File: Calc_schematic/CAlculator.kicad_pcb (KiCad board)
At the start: 2 copper layers, 1 part, among them U2 LCD-016N002L

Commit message: last mod
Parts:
- added J1: Conn_01x02_Female, Connector_JST:JST_PH_B2B-PH-K_1x02_P2.00mm_Vertical, F.Cu at (63.2, 25.2)
- added SW0: SW_Push, Button_Switch_THT:SW_PUSH_6mm_H5mm, F.Cu at (40.8, 109.5)
- added SW1: SW_Push, Button_Switch_THT:SW_PUSH_6mm_H5mm, F.Cu at (40.5, 123.2)
- added SW10: SW_Push, Button_Switch_THT:SW_PUSH_6mm_H5mm, F.Cu at (86.0, 109.5)
- added SW11: SW_Push, Button_Switch_THT:SW_PUSH_6mm_H5mm, F.Cu at (86.2, 123.2)
- added SW12: SW_Push, Button_Switch_THT:SW_PUSH_6mm_H5mm, F.Cu at (86.2, 137.5)
- added SW13: SW_Push, Button_Switch_THT:SW_PUSH_6mm_H5mm, F.Cu at (86.2, 152.2)
- added SW14: SW_Push, Button_Switch_THT:SW_PUSH_6mm_H5mm, F.Cu at (86.5, 166.0)
- added SW15: SW_Push, Button_Switch_THT:SW_PUSH_6mm_H5mm, F.Cu at (106.2, 109.5)
- added SW16: SW_Push, Button_Switch_THT:SW_PUSH_6mm_H5mm, F.Cu at (106.2, 123.2)
- added SW17: SW_Push, Button_Switch_THT:SW_PUSH_6mm_H5mm, F.Cu at (106.2, 137.5)
- added SW18: SW_Push, Button_Switch_THT:SW_PUSH_6mm_H5mm, F.Cu at (106.0, 152.2)
- added SW19: SW_Push, Button_Switch_THT:SW_PUSH_6mm_H5mm, F.Cu at (105.8, 166.0)
- added SW2: SW_Push, Button_Switch_THT:SW_PUSH_6mm_H5mm, F.Cu at (40.5, 137.8)
- added SW20: SW_Push, Button_Switch_THT:SW_PUSH_6mm_H5mm, F.Cu at (129.5, 109.8)
- added SW21: SW_Push, Button_Switch_THT:SW_PUSH_6mm_H5mm, F.Cu at (129.2, 123.2)
- added SW22: SW_Push, Button_Switch_THT:SW_PUSH_6mm_H5mm, F.Cu at (129.8, 137.5)
- added SW23: SW_Push, Button_Switch_THT:SW_PUSH_6mm_H5mm, F.Cu at (130.0, 152.0)
- added SW24: SW_Push, Button_Switch_THT:SW_PUSH_6mm_H5mm, F.Cu at (130.0, 166.0)
- added SW3: SW_Push, Button_Switch_THT:SW_PUSH_6mm_H5mm, F.Cu at (40.5, 152.2)
- added SW4: SW_Push, Button_Switch_THT:SW_PUSH_6mm_H5mm, F.Cu at (40.0, 166.0)
- added SW5: SW_Push, Button_Switch_THT:SW_PUSH_6mm_H5mm, F.Cu at (64.5, 109.5)
- added SW6: SW_Push, Button_Switch_THT:SW_PUSH_6mm_H5mm, F.Cu at (64.5, 123.2)
- added SW7: SW_Push, Button_Switch_THT:SW_PUSH_6mm_H5mm, F.Cu at (64.2, 137.8)
- added SW8: SW_Push, Button_Switch_THT:SW_PUSH_6mm_H5mm, F.Cu at (64.0, 152.2)
- added SW9: SW_Push, Button_Switch_THT:SW_PUSH_6mm_H5mm, F.Cu at (64.0, 166.0)
- added U1: Pico, MCU_RaspberryPi_and_Boards:RPi_Pico_SMD_TH, F.Cu at (73.5, 68.8)
- added U3: AP2112K-3.3, Package_TO_SOT_SMD:SOT-23-5, F.Cu at (75.6, 25.7)
- U2: value LCD-016N002L -> PCF8574TS; footprint Display:LCD-016N002L -> Package_SO:SSOP-20_4.4x6.5mm_P0.65mm
- moved U2 194.2 mm to (43.0, 90.5), turned to 90 degrees
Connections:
- U2 pad 15: unconnected-(U2-Pad15) -> GND
- U2 pad 2: unconnected-(U2-Pad2) -> /SCL
- U2 pad 4: unconnected-(U2-Pad4) -> /SDA
- U2 pad 5: unconnected-(U2-Pad5) -> /5V

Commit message: updated i2c controller
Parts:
- removed U2: PCF8574TS, Package_SO:SSOP-20_4.4x6.5mm_P0.65mm
- added J2: Conn_01x04_Male, Connector_PinHeader_2.54mm:PinHeader_1x04_P2.54mm_Vertical, F.Cu at (27.9, 83.8)
- U1: moved to B.Cu
- moved U1 0.23 mm to (73.7, 68.6), turned to -90 degrees
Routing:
- net /Col4: track 0.00 -> 15.1 mm

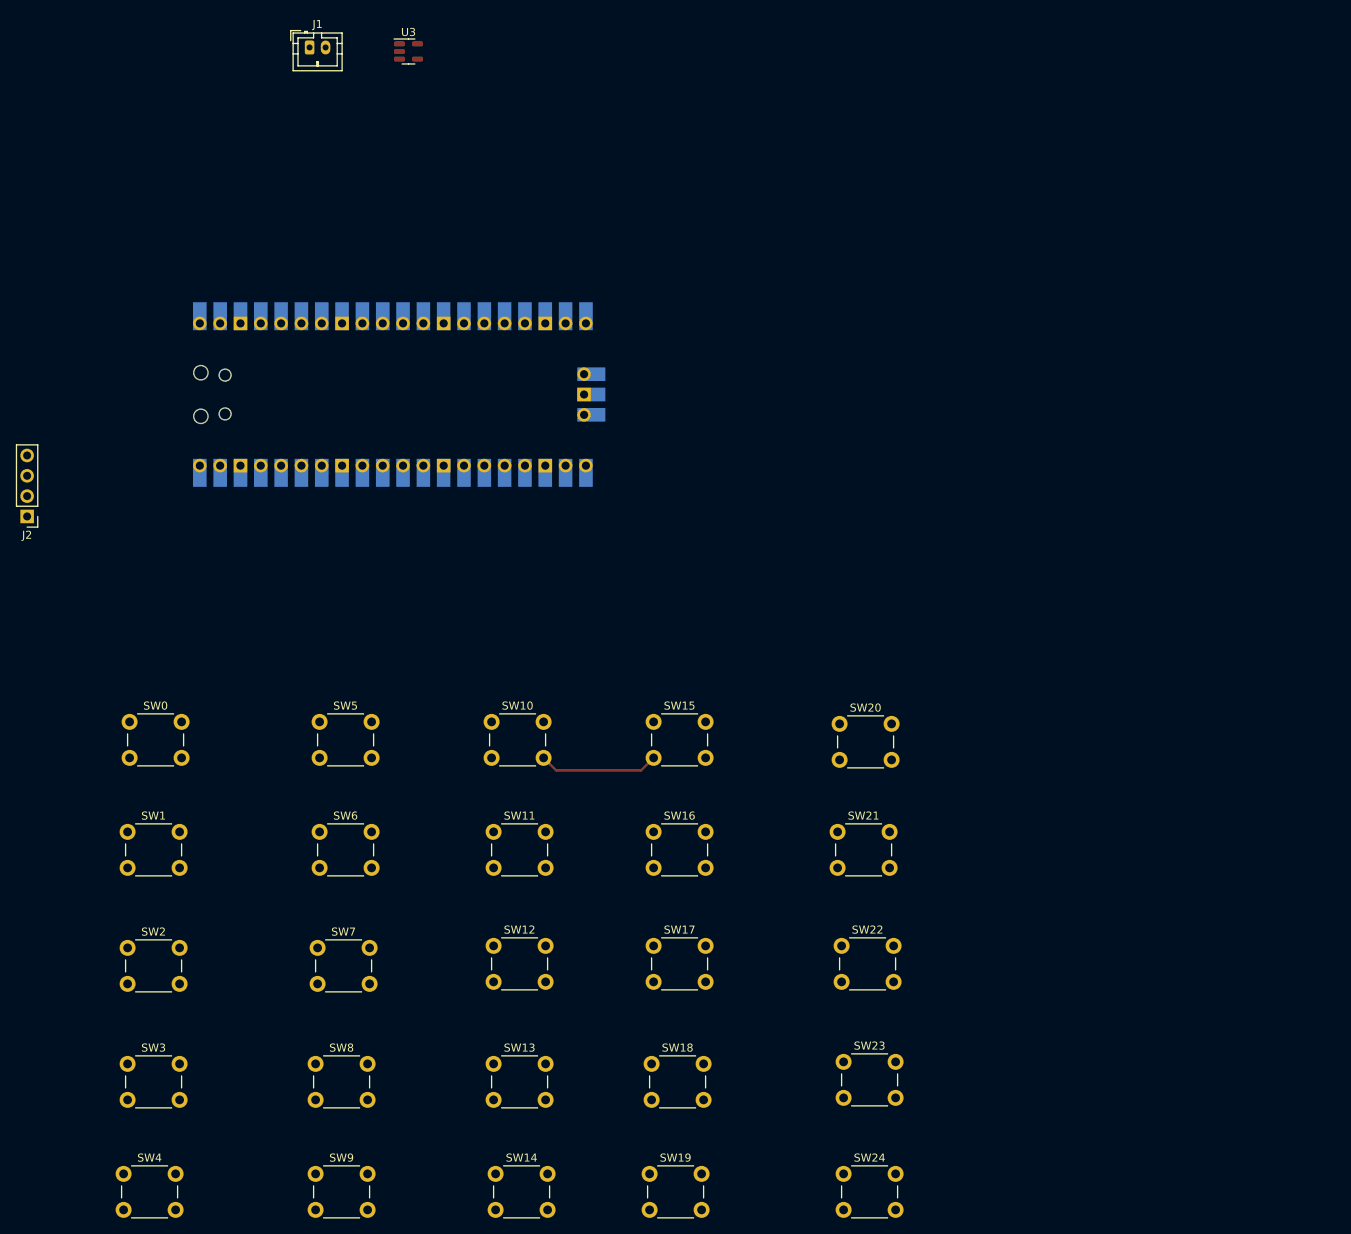
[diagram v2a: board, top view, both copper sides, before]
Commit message: most pins connected except Vbus and ground
Going to use ground plane so no need to connect ground pins yet
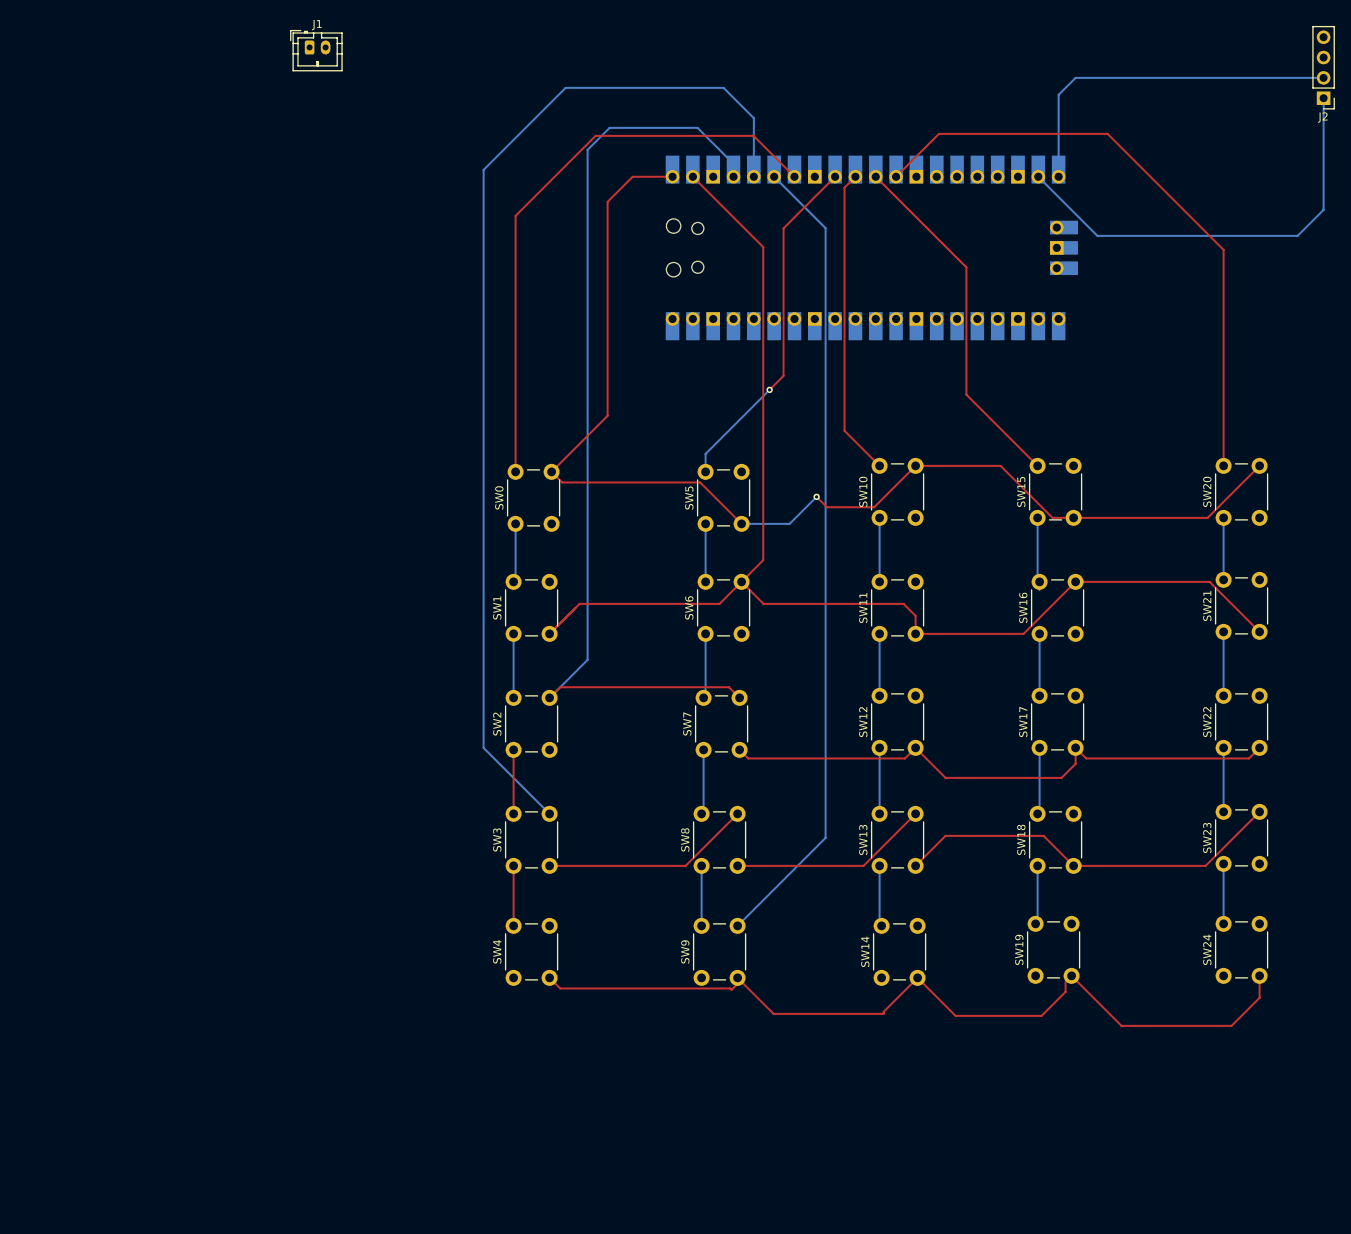
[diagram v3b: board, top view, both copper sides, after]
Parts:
- removed U3: AP2112K-3.3, Package_TO_SOT_SMD:SOT-23-5
- moved J2 170.3 mm to (190.0, 31.5)
- moved U1 61.9 mm to (132.8, 50.2)
- moved SW10 54.8 mm to (134.5, 84.0), turned to 90 degrees
- moved SW4 54.6 mm to (88.8, 141.5), turned to 90 degrees
- moved SW20 54.5 mm to (177.5, 84.0), turned to 90 degrees
- moved SW15 54.4 mm to (154.2, 84.0), turned to 90 degrees
- moved SW21 54.3 mm to (177.5, 98.2), turned to 90 degrees
- moved SW0 54.2 mm to (89.0, 84.8), turned to 90 degrees
- moved SW1 54.2 mm to (88.8, 98.5), turned to 90 degrees
- moved SW11 54.2 mm to (134.5, 98.5), turned to 90 degrees
- moved SW12 54.2 mm to (134.5, 112.8), turned to 90 degrees
- moved SW13 54.2 mm to (134.5, 127.5), turned to 90 degrees
- moved SW16 54.2 mm to (154.5, 98.5), turned to 90 degrees
- moved SW17 54.2 mm to (154.5, 112.8), turned to 90 degrees
- moved SW18 54.2 mm to (154.2, 127.5), turned to 90 degrees
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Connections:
- SW0 pad 2: /Col4 -> /Row1
- SW10 pad 1: Net-(SW10-Pad1) -> /Col3
- SW10 pad 2: /Col4 -> /Row1
- SW11 pad 1: Net-(SW10-Pad1) -> /Col3
- SW12 pad 1: Net-(SW10-Pad1) -> /Col3
- SW13 pad 1: Net-(SW10-Pad1) -> /Col3
- SW14 pad 1: Net-(SW10-Pad1) -> /Col3
- SW15 pad 1: /Col3 -> /Col4
- SW15 pad 2: /Col4 -> /Row1
- SW16 pad 1: /Col3 -> /Col4
- SW17 pad 1: /Col3 -> /Col4
- SW18 pad 1: /Col3 -> /Col4
- SW19 pad 1: /Col3 -> /Col4
- SW20 pad 2: /Col4 -> /Row1
- SW5 pad 2: /Col4 -> /Row1
- U1 pad 1: /Col4 -> /Row1
- U1 pad 18: unconnected-(U1-Pad18) -> GND
- U1 pad 23: unconnected-(U1-Pad23) -> GND
- U1 pad 38: unconnected-(U1-Pad38) -> GND
- U1 pad 40: unconnected-(U1-Pad40) -> /5V
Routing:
- net /Row4: track 0.00 -> 230.9 mm
- net /Row5: track 0.00 -> 205.7 mm
- net /Row3: track 0.00 -> 189.5 mm
- net /Row2: track 0.00 -> 160.7 mm
- net /Row1: track 0.00 -> 146.9 mm, vias 0 -> 1
- net /Col5: track 0.00 -> 107.4 mm
- net /Col1: track 0.00 -> 104.0 mm
- net /Col2: track 0.00 -> 74.6 mm, vias 0 -> 1
- net /Col3: track 0.00 -> 70.1 mm
- net /Col4: track 15.1 -> 77.1 mm
- net /SDA: track 0.00 -> 54.0 mm
- net /SCL: track 0.00 -> 44.2 mm

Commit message: final CAD
board sent to FaB
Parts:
- added R1: R, SamacSys_Parts:RESC3216X60N, B.Cu at (140.0, 114.8)
- added R10: R, SamacSys_Parts:RESC3216X60N, B.Cu at (120.4, 130.6)
- added R2: R, SamacSys_Parts:RESC3216X60N, B.Cu at (92.8, 93.8)
- added R3: R, SamacSys_Parts:RESC3216X60N, B.Cu at (102.8, 129.9)
- added R4: R, SamacSys_Parts:RESC3216X60N, B.Cu at (139.6, 86.8)
- added R5: R, SamacSys_Parts:RESC3216X60N, B.Cu at (100.6, 144.5)
- added R6: R, SamacSys_Parts:RESC3216X60N, B.Cu at (120.6, 144.2)
- added R7: R, SamacSys_Parts:RESC3216X60N, B.Cu at (130.4, 144.4)
- added R8: R, SamacSys_Parts:RESC3216X60N, B.Cu at (140.1, 128.6)
- added R9: R, SamacSys_Parts:RESC3216X60N, B.Cu at (139.4, 94.3)
- J1: moved to B.Cu
- moved J1 140.9 mm to (152.0, 134.7), turned to 180 degrees
- moved SW20 45.5 mm to (132.0, 85.1)
- moved SW22 45.5 mm to (132.0, 111.8)
- moved SW24 45.5 mm to (132.0, 140.6)
- moved SW21 45.5 mm to (132.0, 98.6)
- moved SW23 45.5 mm to (132.0, 126.3)
- moved J2 34.9 mm to (155.8, 38.5)
- moved SW17 31.5 mm to (123.0, 112.1)
- moved SW16 31.5 mm to (123.0, 98.6)
- moved SW18 31.4 mm to (122.9, 126.0)
- moved SW15 31.3 mm to (123.0, 85.0)
- moved SW19 31.2 mm to (122.8, 140.8)
- moved SW14 20.9 mm to (113.9, 140.9)
- moved SW13 20.6 mm to (114.0, 126.1)
- moved SW10 20.6 mm to (114.0, 84.9)
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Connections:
- J1 pad 1: unconnected-(J1-Pad1) -> /VBAT
- J1 pad 2: unconnected-(J1-Pad2) -> GND
- U1 pad 39: unconnected-(U1-Pad39) -> /VBAT
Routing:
- net /5V: track 0.00 -> 193.0 mm
- net /VBAT: track 0.00 -> 109.8 mm, vias 0 -> 3
- net /Col2: track 74.6 -> 147.2 mm
- net /Row3: track 189.5 -> 140.8 mm
- net /Col5: track 107.4 -> 152.8 mm, vias 0 -> 2
- net /Row1: track 146.9 -> 109.5 mm, vias 1 -> 0
- net /Row5: track 205.7 -> 168.4 mm
- net /SDA: track 54.0 -> 19.5 mm, vias 0 -> 1
- net /Col3: track 70.1 -> 101.2 mm
- net /Col4: track 77.1 -> 101.5 mm
- net /SCL: track 44.2 -> 23.5 mm, vias 0 -> 1
- net /Col1: track 104.0 -> 120.7 mm
- net /Row2: track 160.7 -> 146.0 mm
- net /Row4: track 230.9 -> 222.1 mm
- added copper zone on B.Cu, net GND
- added copper zone on F.Cu, net GND
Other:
- board outline added: 85 x 125 mm
- board text added: "Designed by: Bernadeau Faurestal Ahliah Nordstrom Angelo Maldonado-Liu Ibrahim Zreik"
- board text added: "Group 2"
- board text added: "Pi pico Calculator"
